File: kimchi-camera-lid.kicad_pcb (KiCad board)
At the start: 4 copper layers, 65 x 32 mm, 21 parts, among them J1 DF40HC(3.5)-60DS, J2 DF40HC(3.5)-60DS, J3 DF40C-60DP, J4 DF40C-60DP, J5 Conn_01x15_MountingPin, J6 Conn_01x15_MountingPin, J7 Conn_01x22_MountingPin, J8 Conn_01x02, K1 KIMCHI_MICRO, U1 24C32

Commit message: Complete design for v1.0
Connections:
- J1 pad 11: (no net) -> /P1_11
- J1 pad 51: (no net) -> /P1_51
- J2 pad 42: (no net) -> /P2_42
- J2 pad 54: (no net) -> /P2_54
- J2 pad 58: (no net) -> /P2_58
- J3 pad 11: (no net) -> /P1_11
- J3 pad 51: (no net) -> /P1_51
- J3 pad MP: (no net) -> GND
- J4 pad 42: (no net) -> /P2_42
- J4 pad 54: (no net) -> /P2_54
- J4 pad 58: (no net) -> /P2_58
- J4 pad MP: (no net) -> GND
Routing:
- net GND: track 69.8 -> 120.5 mm
- net (no net): track 9.40 -> 0.00 mm, vias 5 -> 0
- net VDD_3V3: track 28.6 -> 33.4 mm
- net /P2_58: track 0.00 -> 1.88 mm, vias 0 -> 1
- net /P2_54: track 0.00 -> 1.88 mm, vias 0 -> 1
- net /P2_42: track 0.00 -> 1.88 mm, vias 0 -> 1
- net /P1_51: track 0.00 -> 1.88 mm, vias 0 -> 1
- net /P1_11: track 0.00 -> 1.88 mm, vias 0 -> 1
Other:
- board text added: "All tolerances +/-10%. Layers 1, 4 (kimchi-camera-lid-F_Cu.gtl, kimchi-camera-lid-B_Cu.gbl) Single ended: Width: 5 mils Impedance: 50 Ohms Differential: Width / Gap: 4.99 mils / 5.01 mils Impedance: 100 Ohms Layers 2-3 (kimchi-camera-lid-In[1-2]_Cu.g[2-3]) Single ended: Width: 5 mils Impedance: 50 Ohms"
- board text added: "kimχ CSI Camera Lid v1.0"

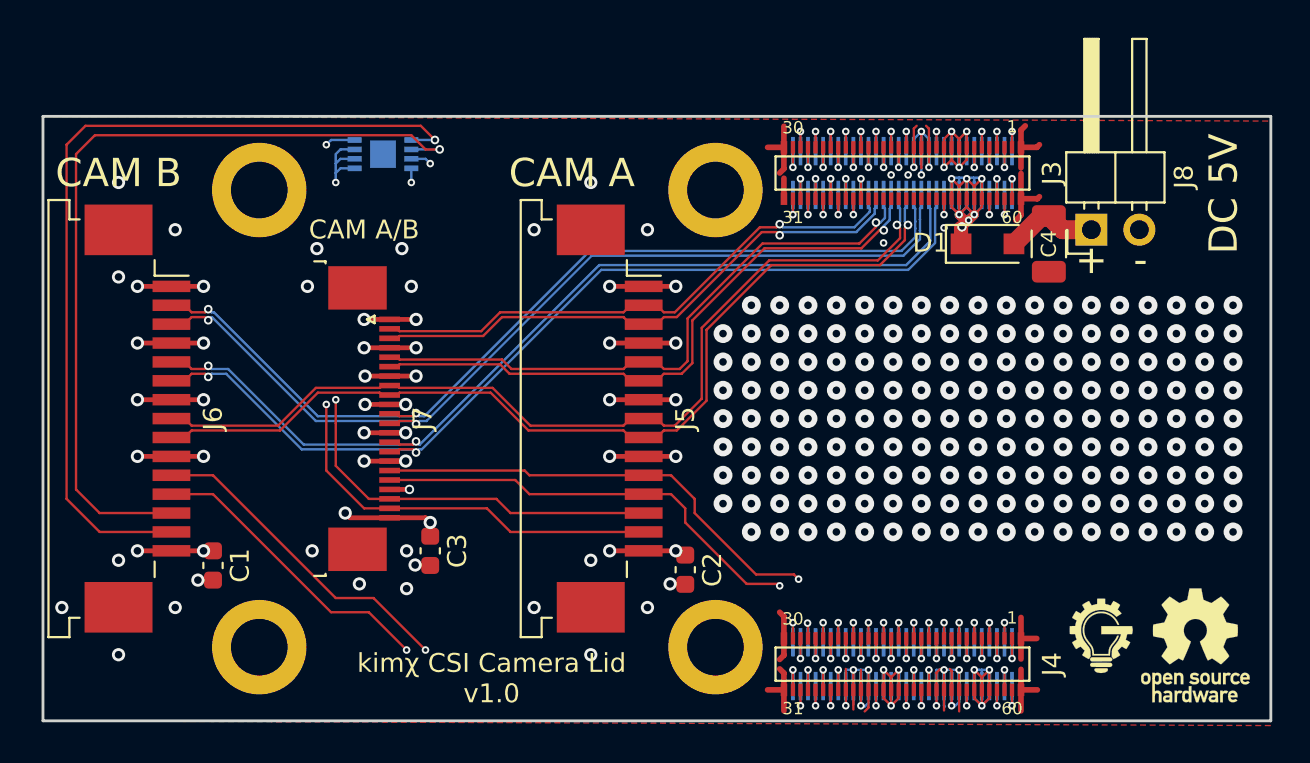
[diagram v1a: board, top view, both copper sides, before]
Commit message: Increase 0.2/0.4 mm via to 0.25/0.5 mm
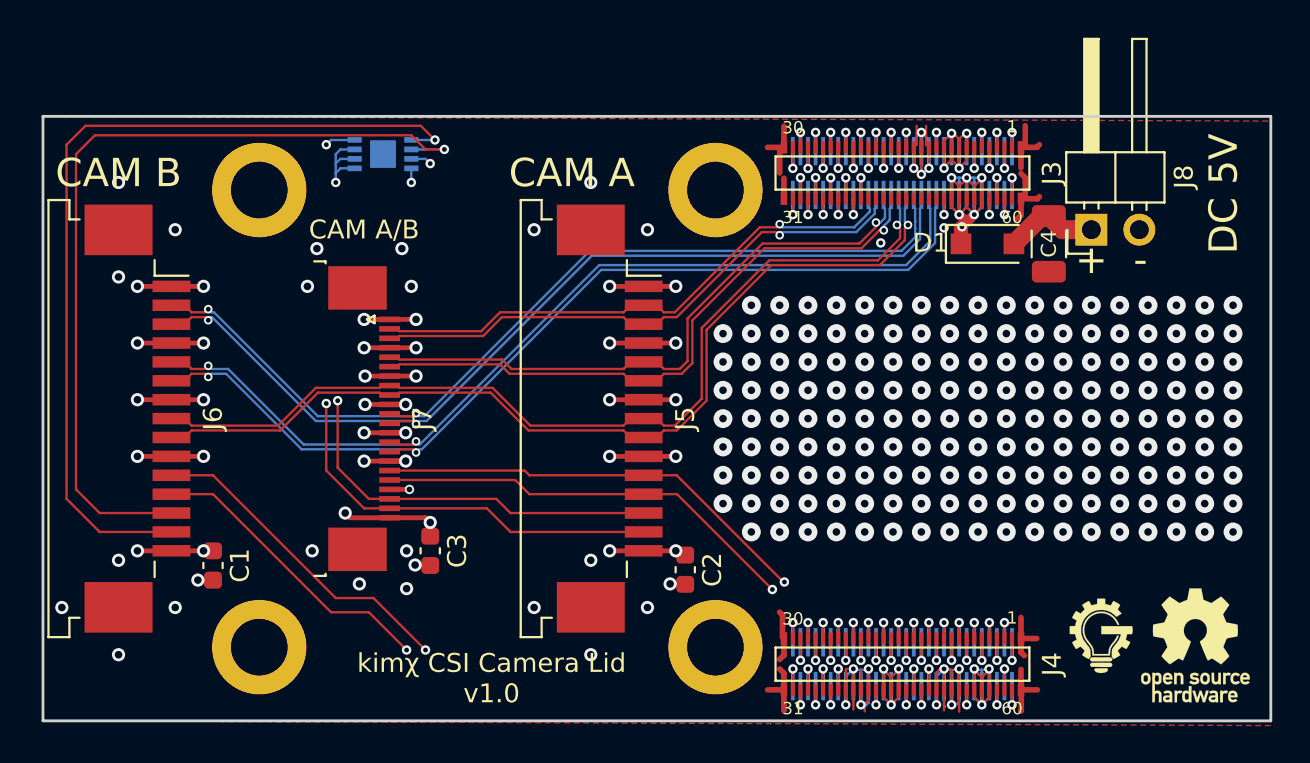
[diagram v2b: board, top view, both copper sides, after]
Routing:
- net SAI3_MCLK: track 32.1 -> 33.8 mm
- net VCHG: track 28.4 -> 28.7 mm, vias 7 -> 6
- net GND: track 120.5 -> 120.3 mm, vias 241 -> 239
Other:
- net class CSI/DSI: via_dia 0.4 -> 0.5; via_drill 0.2 -> 0.25
- net class Default: via_dia 0.4572 -> 0.5; via_drill 0.254 -> 0.25
- net class PCIE removed
- net class USB: via_dia 0.4 -> 0.5; via_drill 0.2 -> 0.25
- rule via_min_drill: 0.1016 -> 0.25
- rule via_min_size: 0.3048 -> 0.4
